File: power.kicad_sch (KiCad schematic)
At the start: 28 parts, among them J2 Barrel_Jack_MountingPin, U1 ST715M25R, U3 ZXCT1107

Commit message: sent to jlcpcb
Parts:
- BAL1: value Conn_01x04 -> Conn_01x04 JST-XH
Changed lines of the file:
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@@
 			)
 		)
-		(property "Value" "Conn_01x04"
+		(property "Value" "Conn_01x04 JST-XH"
 			(at 41.91 44.4499 0)
 			(effects

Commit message: New design and layout
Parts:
- added R31, R32: 220k, Resistor_SMD:R_0402_1005Metric, symbol Device:R
- added R33, R34: 47.5k, Resistor_SMD:R_0402_1005Metric, symbol Device:R
- C12, C13: value 1n -> .1u; LCSC_Code C1588 -> C14663
- R10: value 39k -> 47.5k; footprint Resistor_SMD:R_0603_1608Metric -> Resistor_SMD:R_0402_1005Metric; LCSC_Code C23153 -> C319604; Tolerance (none) -> 0.5%
- R4: value 0.25 -> 0.1; LCSC_Code C49283 -> C2903496
- R6: value 1.2k -> 3k; LCSC_Code C22765 -> C4211
- R7: value 200k -> 220k; footprint Resistor_SMD:R_0603_1608Metric -> Resistor_SMD:R_0402_1005Metric; LCSC_Code C25811 -> C851925; Tolerance (none) -> 0.5%
- R8: value 39k -> 220k; footprint Resistor_SMD:R_0603_1608Metric -> Resistor_SMD:R_0402_1005Metric; LCSC_Code C23153 -> C851925; Tolerance (none) -> 0.5%
- R9: value 200k -> 47.5k; footprint Resistor_SMD:R_0603_1608Metric -> Resistor_SMD:R_0402_1005Metric; LCSC_Code C25811 -> C319604; Tolerance (none) -> 0.5%
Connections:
- net +BATT: now also R8.1
- net GND: now also R9.1, R33.1, R34.1; no longer R8.1
- net VBATT_ADC: now also R10.2, R9.2
- net VSOLAR: now also R31.1, R32.1; no longer R9.1
- net VSOLAR_ADC: now also R31.2, R32.2, R33.2, R34.2; no longer R10.2, R9.2
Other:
- note added: "Rsense = .1 ohm, @ 2 amps = 0.2V (Recommended for full range is 0.5V drop, but that's too much) Iout = 0.004 * Vsense so 3000 * .004*.2 = 2.4V @ 2 amps current"
- note added: "Using || higher precision resistors to reduce absolute error on balancing Also, each divider uses the same range (even the 1S and 2S ones), so that you have consistency. 110k || 23.75k => 19.5k impedance 19.5k ohm * 0.1u cap = 2ms 12*(47.5/(47.5+220)) ~= 2.1V"
- note removed: "12V * (39/239) ~= 2V"
- note removed: "Rsense = .25 ohm, @ 2 amps = 0.5V Iout = 0.004 * Vsense so 1200 * 0.002 = 2.4V @ 2 amps current"

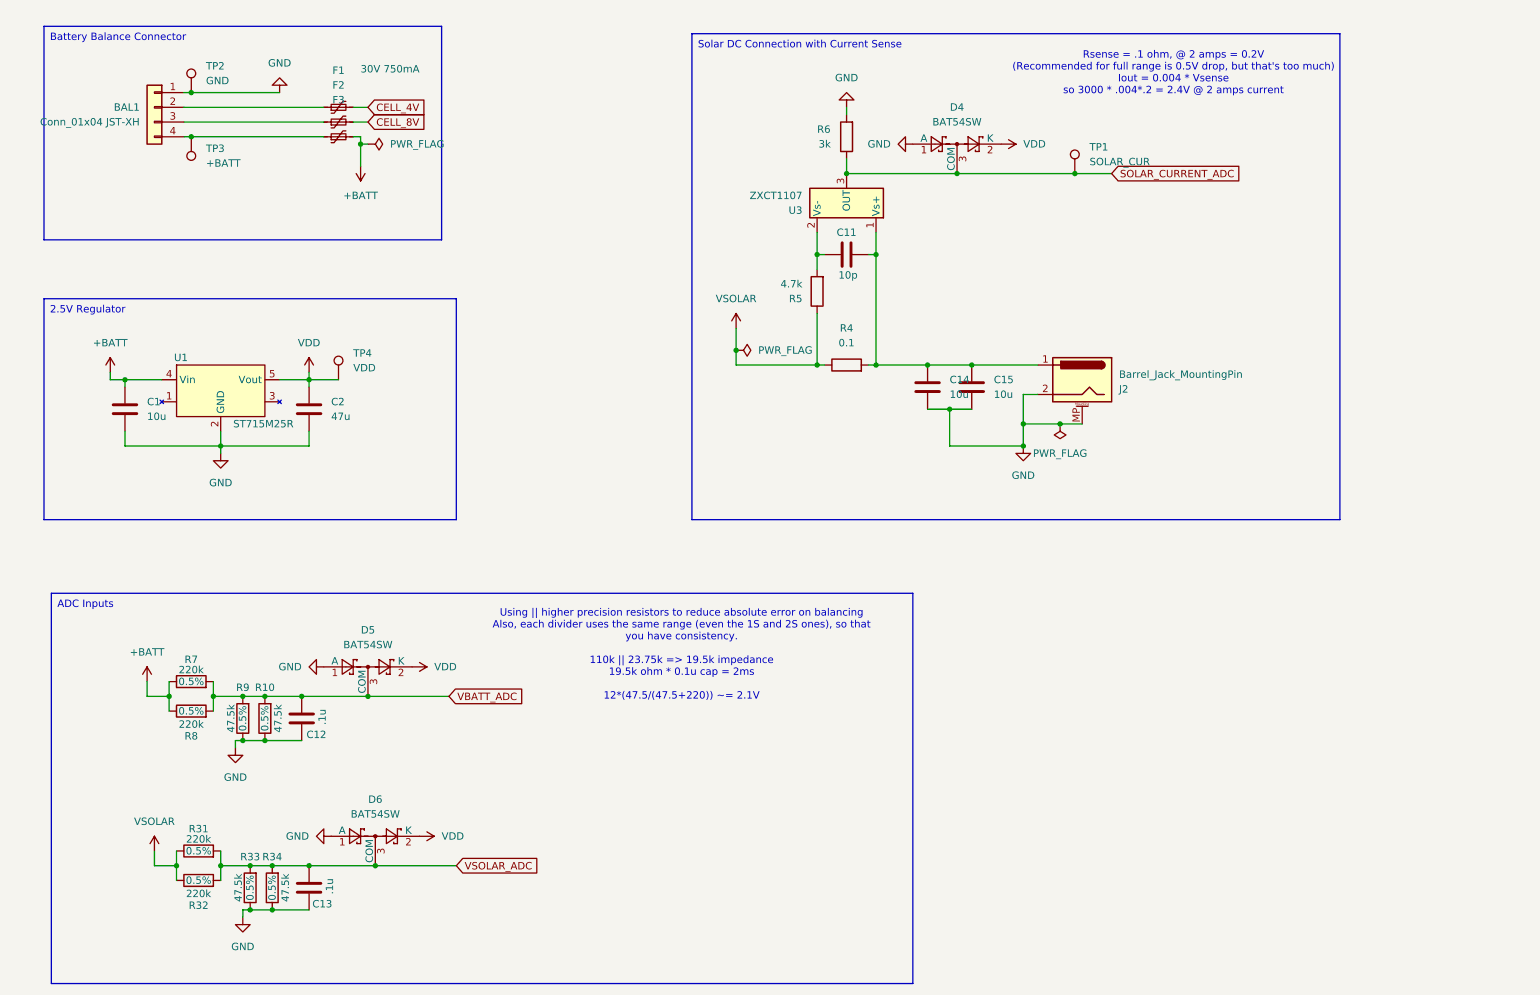
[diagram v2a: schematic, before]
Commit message: Better balance resistors, fixes
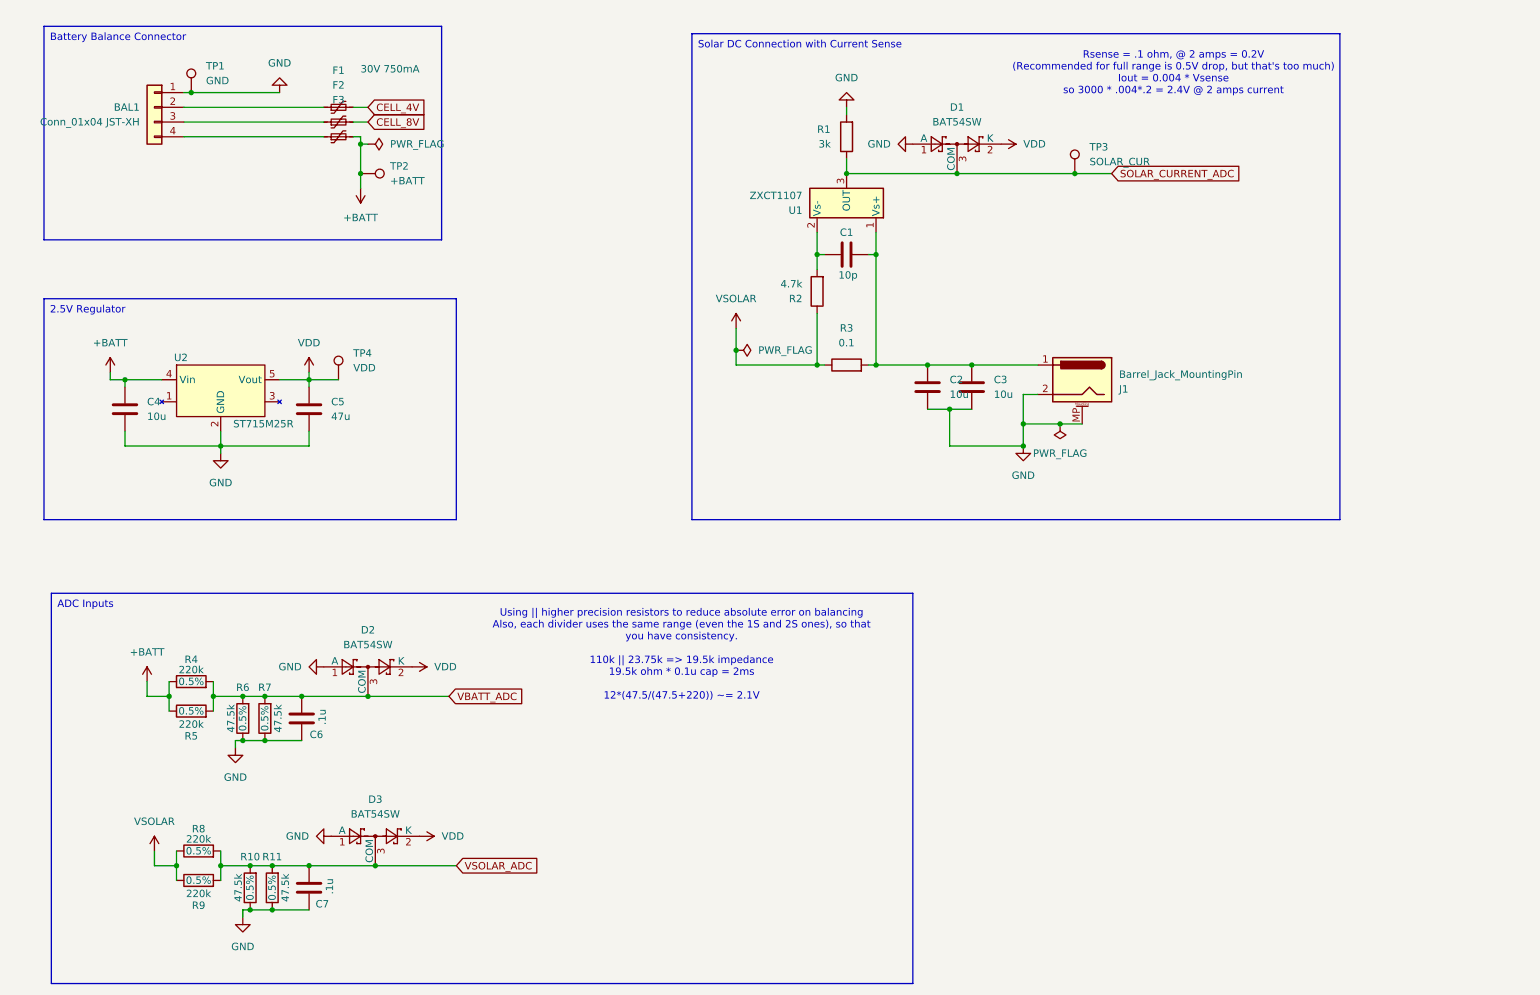
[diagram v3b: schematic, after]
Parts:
- renumbered C11 to C1, C14 to C2, C15 to C3, C1 to C4, C2 to C5, C12 to C6, C13 to C7, D4 to D1, D5 to D2, D6 to D3, J2 to J1, R6 to R1, R33 to R10, R34 to R11, R5 to R2, R4 to R3, R7 to R4, R8 to R5, R9 to R6, R10 to R7, R31 to R8, R32 to R9, TP2 to TP1, TP3 to TP2, TP1 to TP3, U3 to U1, U1 to U2
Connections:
- net +BATT: now also TP2.1
- net at BAL1.4 (Pin_4), F3.1: no longer TP2.1
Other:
- moved on the sheet: TP2

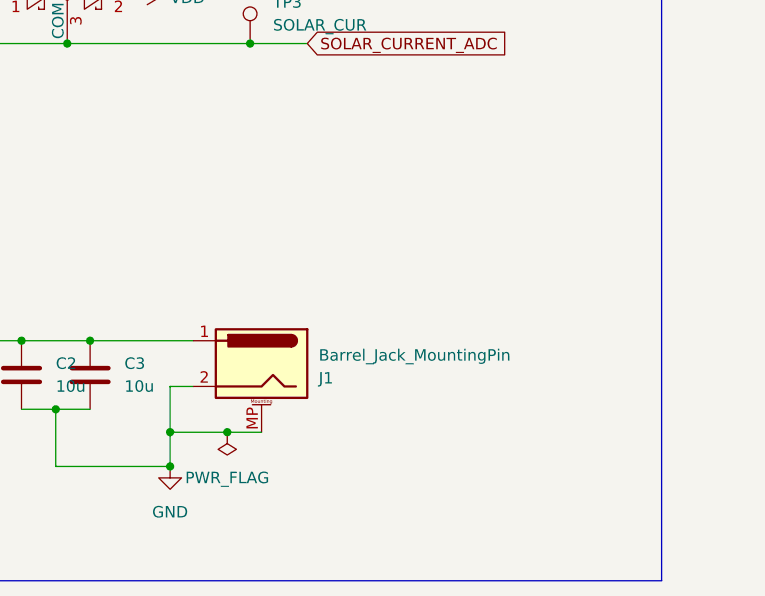
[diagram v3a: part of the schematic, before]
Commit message: Added plugged in detection
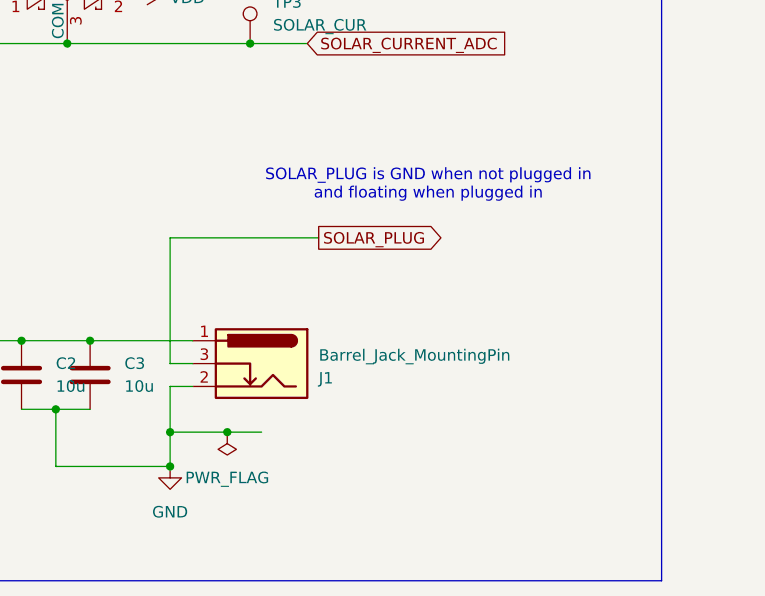
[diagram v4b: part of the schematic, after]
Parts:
- J1: symbol Connector:Barrel_Jack_MountingPin -> Connector:Barrel_Jack_Switch
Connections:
- net GND: no longer J1.MP (MountPin)
- new net SOLAR_PLUG: J1.3
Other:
- note added: "SOLAR_PLUG is GND when not plugged in and floating when plugged in"
- moved on the sheet: J1
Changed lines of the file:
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@@
+	(wire
+		(pts
+			(xy 194.31 88.9) (xy 194.31 74.93)
+		)
+		(stroke
+			(width 0)
+			(type default)
+		)
+	)
 	(wire
 		(pts
@@
 	(wire
 		(pts
+			(xy 194.31 74.93) (xy 210.82 74.93)
+		)
+		(stroke
+			(width 0)
+			(type default)
+		)
+	)
+	(wire
+		(pts
 			(xy 144.78 80.01) (xy 144.78 83.82)
 		)
@@
 		(pts
 			(xy 158.75 86.36) (xy 160.02 86.36)
+		)
+		(stroke
+			(width 0)
+			(type default)
+		)
+	)
+	(wire
+		(pts
+			(xy 196.85 88.9) (xy 194.31 88.9)
 		)
 		(stroke
@@
 			)
 			(justify left top)
+		)
+	)
+	(text "SOLAR_PLUG is GND when not plugged in\nand floating when plugged in"
+		(exclude_from_sim no)
+		(at 223.012 69.088 0)
+		(effects
+			(font
+				(size 1.27 1.27)
+			)
 		)
 	)
@@
 					(size 1.27 1.27)
 				)
+				(hide yes)
+			)
+		)
+	)
+	(global_label "SOLAR_PLUG"
+		(shape output)
+		(at 210.82 74.93 0)
+		(fields_autoplaced yes)
+		(effects
+			(font
+				(size 1.27 1.27)
+			)
+			(justify left)
+		)
+		(property "Intersheetrefs" "${INTERSHEET_REFS}"
+			(at 225.5981 74.93 0)
+			(effects
+				(font
+					(size 1.27 1.27)
+				)
+				(justify left)
 				(hide yes)
 			)
@@
 	)
 	(symbol
-		(lib_id "Connector:Barrel_Jack_MountingPin")
+		(lib_id "Connector:Barrel_Jack_Switch")
 		(at 204.47 88.9 0)
 		(mirror y)
@@
 			)
 		)
-		(property "Description" "DC Barrel Jack with a mounting pin"
+		(property "Description" "DC Barrel Jack with switch"
 			(at 204.47 88.9 0)
 			(effects
@@
 		(pin "2"
 		)
-		(pin "MP"
+		(pin "3"
 		)
 		(instances

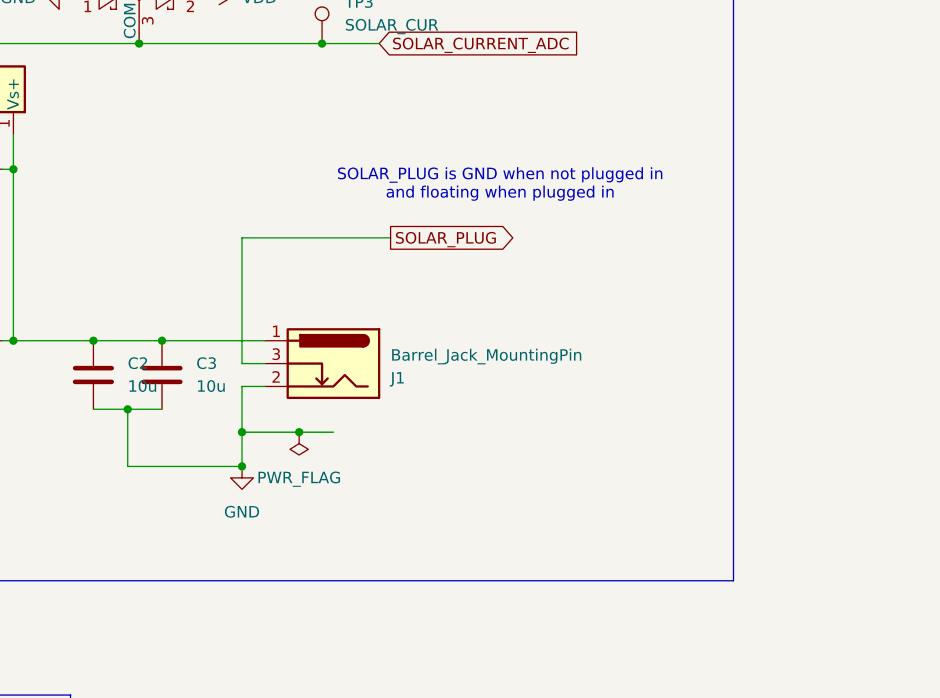
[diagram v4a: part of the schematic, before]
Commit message: Adding notes, solder jumpers for picking polarity of dc plugs
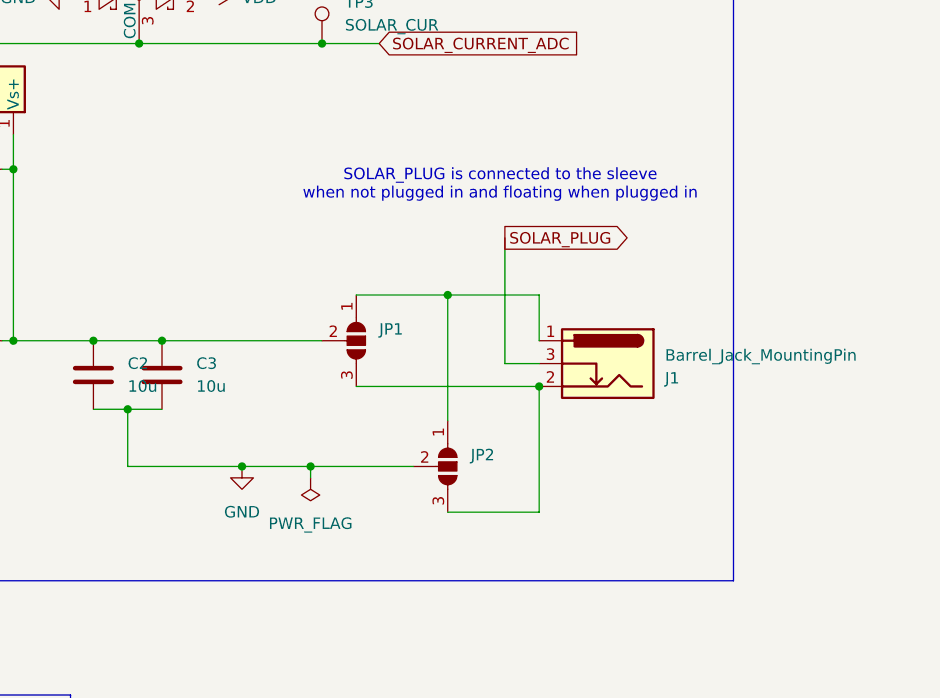
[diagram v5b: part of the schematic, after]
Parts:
- added JP1, JP2: SolderJumper_3_Open, Jumper:SolderJumper-3_P2.0mm_Open_TrianglePad1.0x1.5mm_NumberLabels, symbol Jumper:SolderJumper_3_Open
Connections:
- net GND: now also JP2.2 (C); no longer J1.2
- net at C1.1, C2.1, C3.1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: now also JP1.2 (C); no longer J1.1
- new net: J1.1, JP1.1 (A), JP2.1 (A)
- new net: J1.2, JP1.3 (B), JP2.3 (B)
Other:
- note added: "SOLAR_PLUG is connected to the sleeve when not plugged in and floating when plugged in"
- note removed: "SOLAR_PLUG is GND when not plugged in and floating when plugged in"
- moved on the sheet: J1

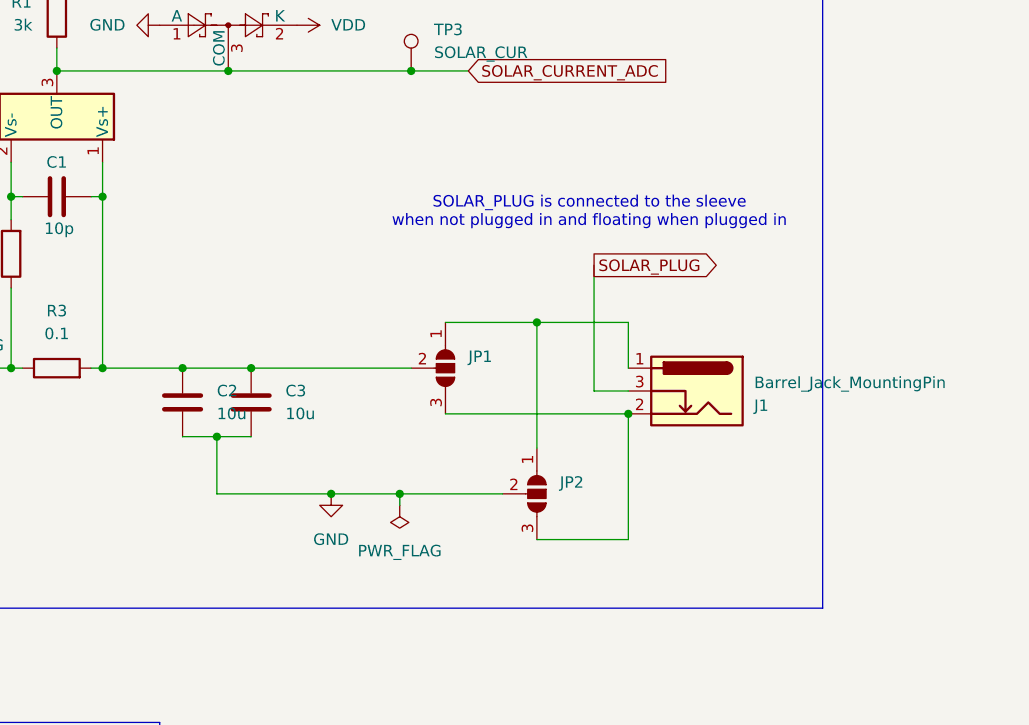
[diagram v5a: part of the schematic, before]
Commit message: Adding XT30 solar connector
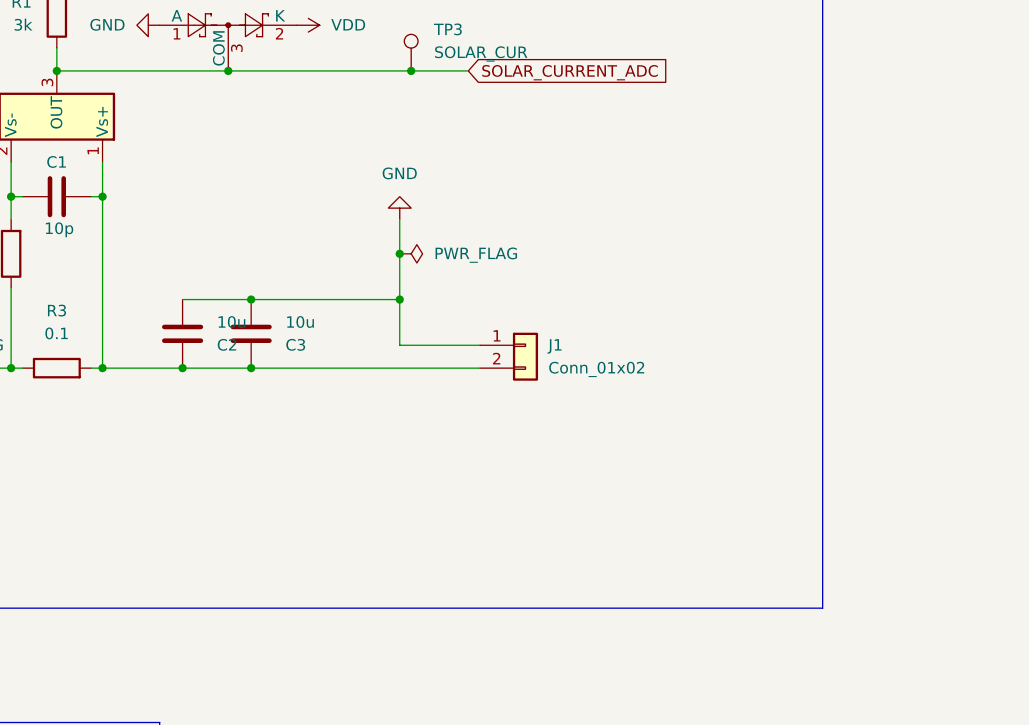
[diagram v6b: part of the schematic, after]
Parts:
- removed J1: Barrel_Jack_MountingPin, Connector_BarrelJack:BarrelJack_Horizontal, symbol Connector:Barrel_Jack_Switch
- removed JP1, JP2: SolderJumper_3_Open, Jumper:SolderJumper-3_P2.0mm_Open_TrianglePad1.0x1.5mm_NumberLabels, symbol Jumper:SolderJumper_3_Open
- added J1: Conn_01x02, Connector_AMASS:AMASS_XT30PW-M_1x02_P2.50mm_Horizontal, symbol Connector_Generic:Conn_01x02
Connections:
- net GND: now also J1.1 (Pin_1)
- net at C1.1, C2.1, C3.1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: now also J1.2 (Pin_2)
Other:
- note removed: "SOLAR_PLUG is connected to the sleeve when not plugged in and floating when plugged in"
- moved on the sheet: C2, C3
